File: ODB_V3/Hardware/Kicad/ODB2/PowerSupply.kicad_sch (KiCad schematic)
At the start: 54 parts, among them J15 Vin_XT30PW-F, U13 L6981N33DR, U7 MPQ9843GLE-5-AEC1-Z

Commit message: wip: 3v3 buck
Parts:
- removed NT3: NetTie_2, NetTie:NetTie-2_SMD_Pad0.5mm, symbol Device:NetTie_2
- 3V3_C1, 3V3_C10, 3V3_C2: footprint Capacitor_SMD:C_1210_3225Metric -> Capacitor_SMD:C_0603_1608Metric
- NT4: footprint NetTie:NetTie-2_SMD_Pad0.5mm -> NetTie:NetTie-4_SMD_Pad0.5mm

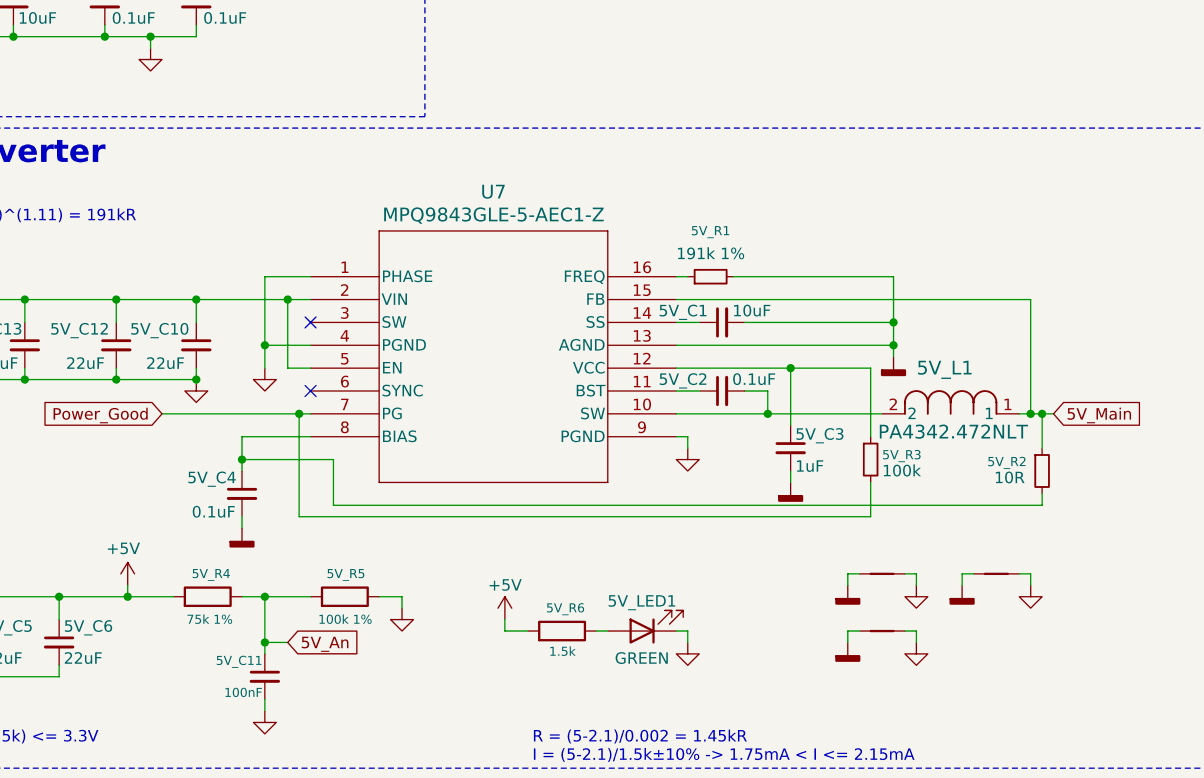
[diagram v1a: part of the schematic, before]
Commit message: feat: add good power input to stm32 + add pull-up 3v3 to good power
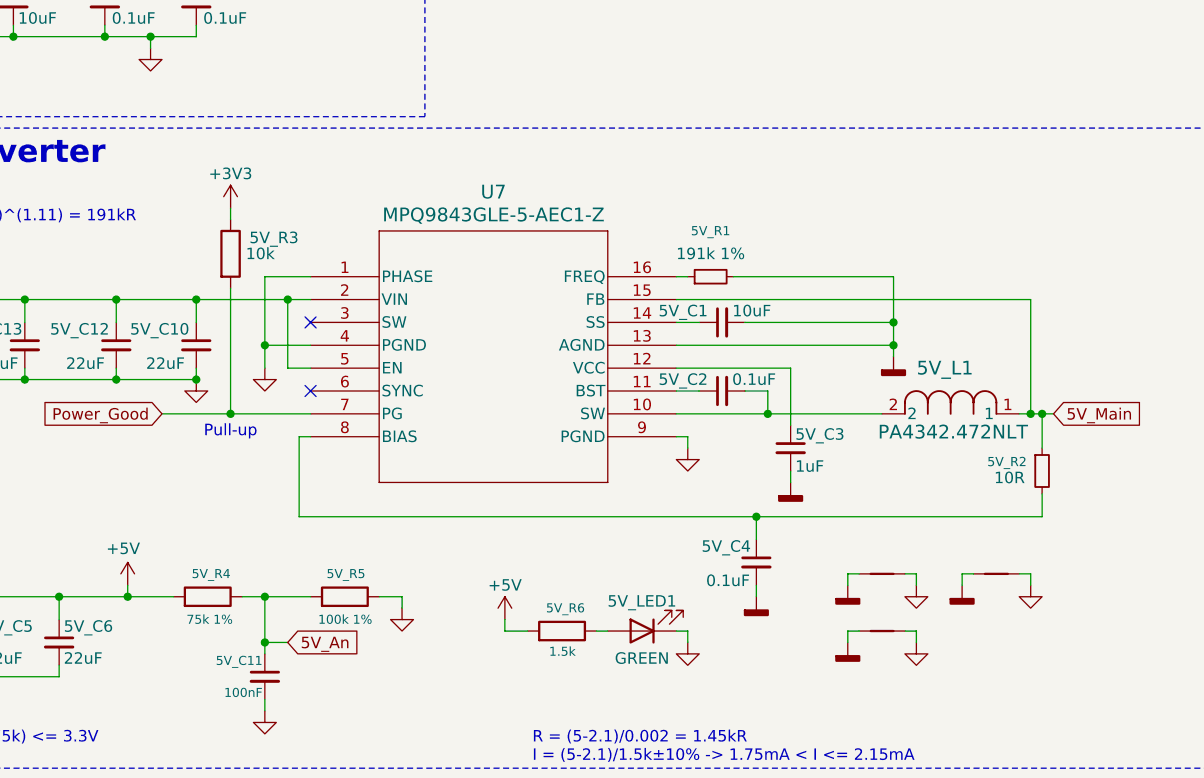
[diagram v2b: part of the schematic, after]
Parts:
- removed 5V_R3: 100k, Resistor_SMD:R_0603_1608Metric, symbol Device:R_Small
- added 5V_R3: 10k, Resistor_SMD:R_0603_1608Metric, symbol Device:R
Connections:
- net +3V3: now also 5V_R3.1
- net Power_Good: now also 5V_R3.2
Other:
- note added: "Pull-up"
- moved on the sheet: 5V_C4

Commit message: wip: pyro trace
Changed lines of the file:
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@@
 	(rectangle
 		(start 15.24 52.07)
-		(end 205.74 123.19)
+		(end 176.53 123.19)
 		(stroke
 			(width 0)

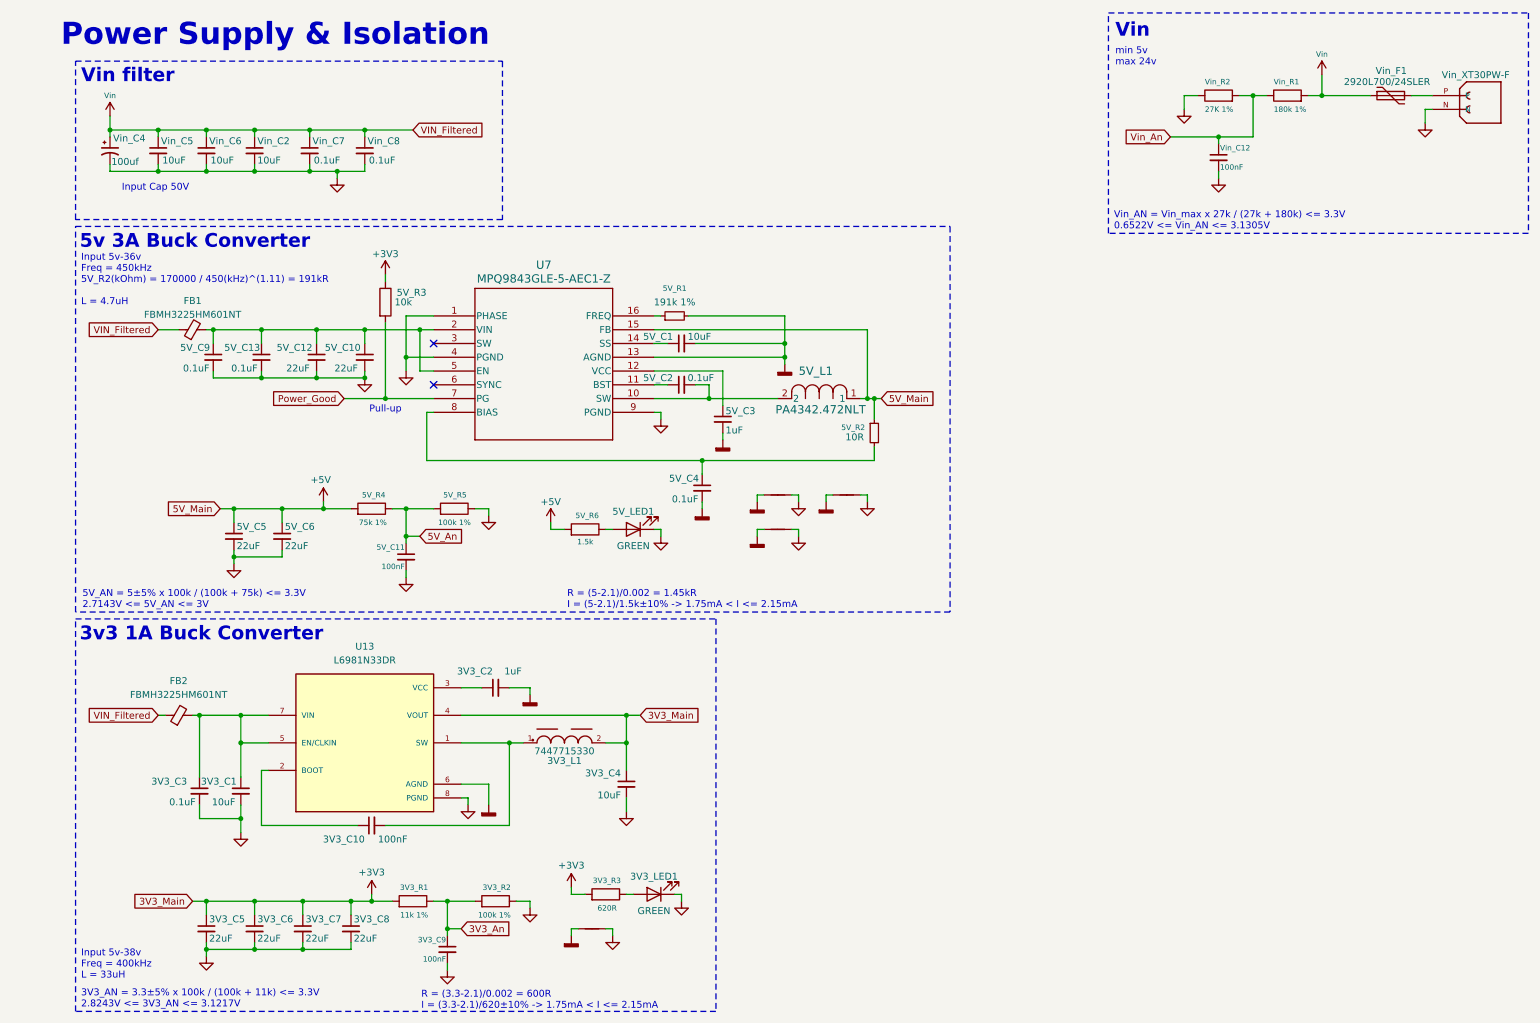
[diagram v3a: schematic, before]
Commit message: wip: change red critical LED to AAKK RG LED + fixes
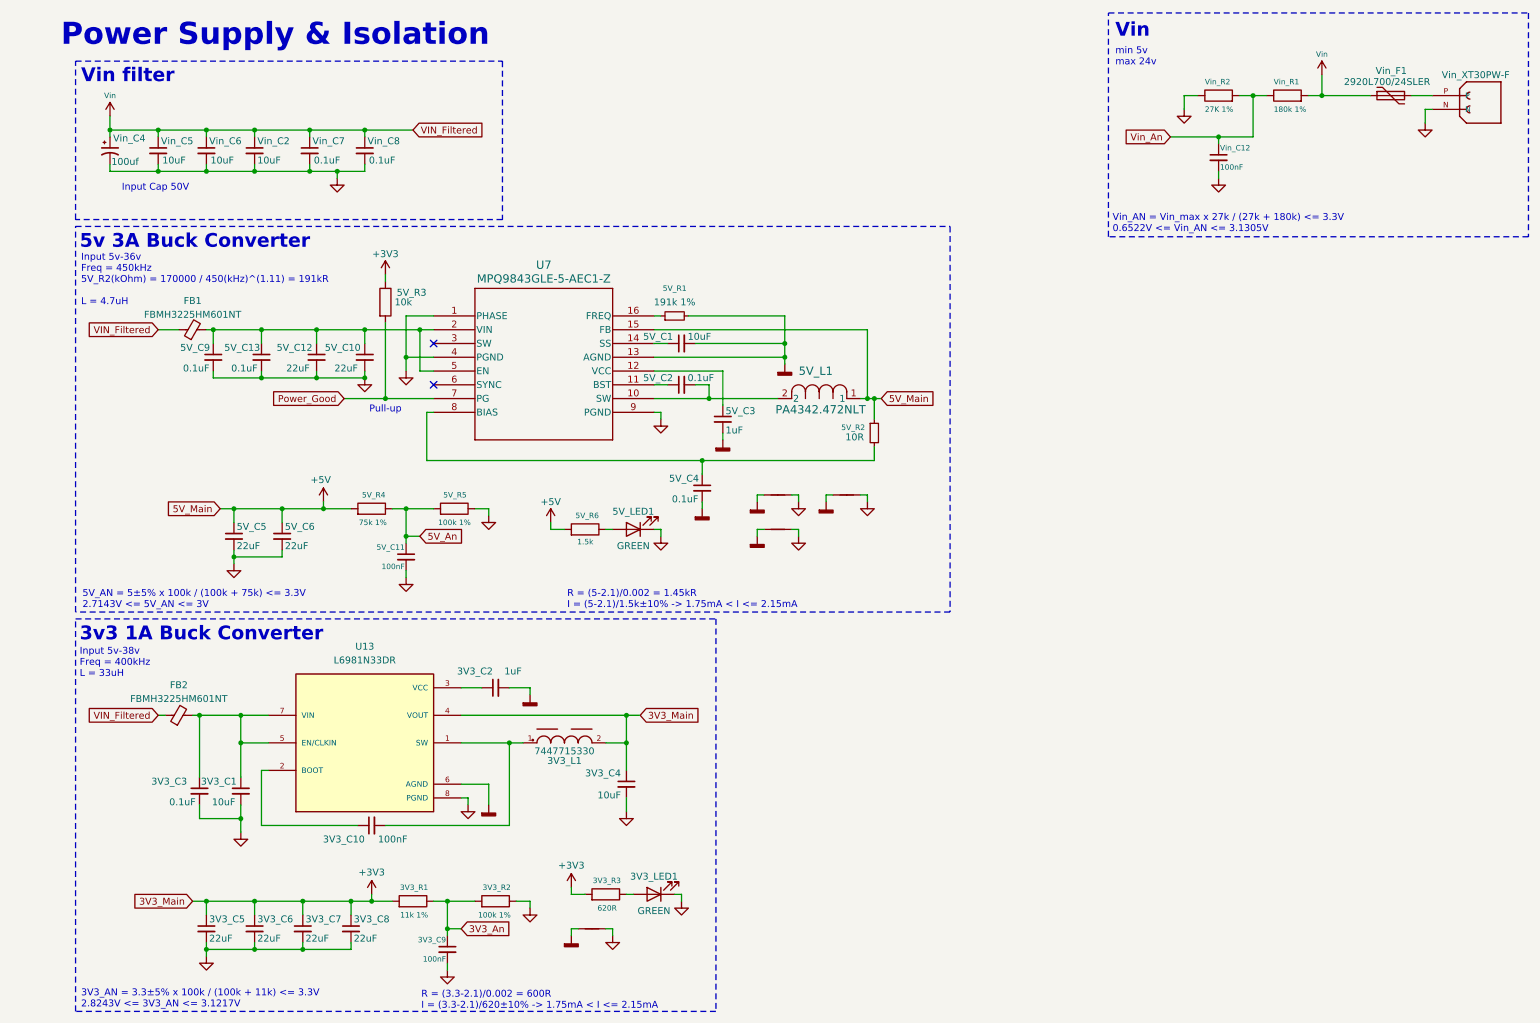
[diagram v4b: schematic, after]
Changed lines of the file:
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@@
 	(rectangle
 		(start 205.74 12.7)
-		(end 283.21 53.34)
+		(end 283.21 53.975)
 		(stroke
 			(width 0)
@@
 	(text "Input 5v-38v\nFreq = 400kHz\nL = 33uH"
 		(exclude_from_sim no)
-		(at 16.256 191.008 0)
+		(at 16.002 135.382 0)
 		(effects
 			(font
@@
 	(text "Vin_AN = Vin_max x 27k / (27k + 180k) <= 3.3V\n0.6522V <= Vin_AN <= 3.1305V"
 		(exclude_from_sim no)
-		(at 206.756 51.054 0)
+		(at 206.502 51.562 0)
 		(effects
 			(font
@@
 		(on_board yes)
 		(dnp no)
-		(fields_autoplaced yes)
 		(property "Reference" "FB2"
-			(at 34.2519 135.89 90)
+			(at 34.29 136.652 90)
 			(effects
 				(font
@@
 		)
 		(property "Value" "FBMH3225HM601NT"
-			(at 34.2519 138.43 90)
+			(at 34.29 139.192 90)
 			(effects
 				(font

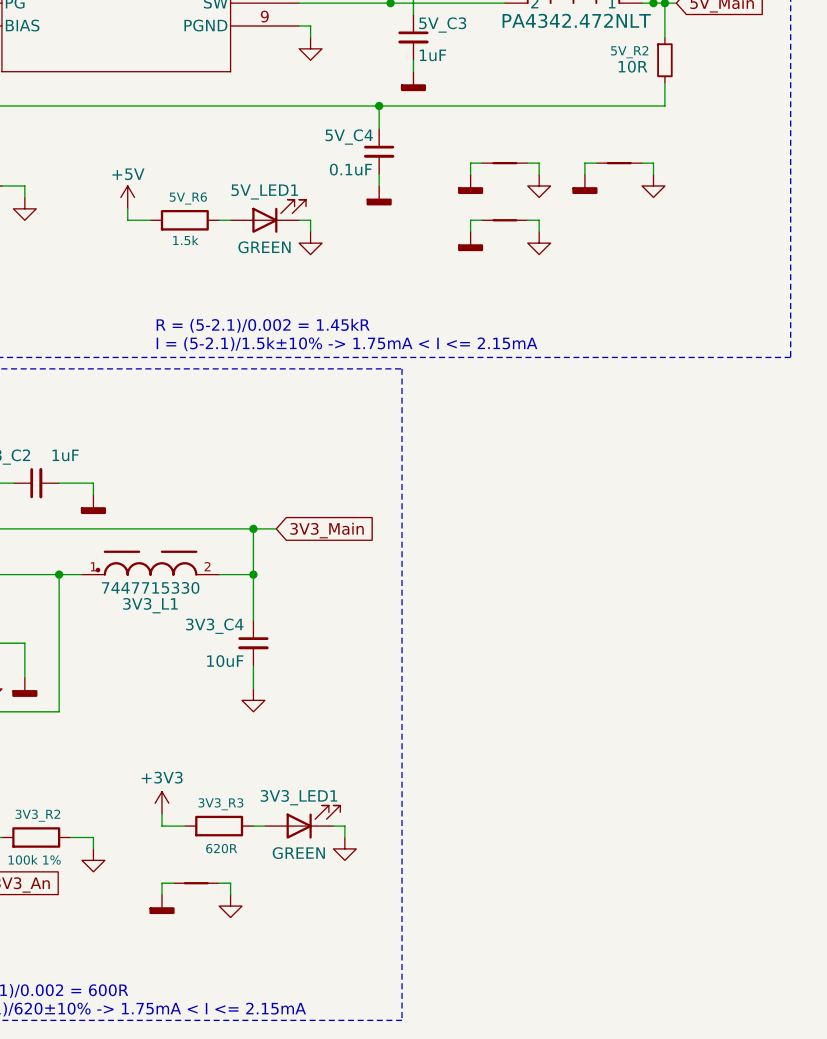
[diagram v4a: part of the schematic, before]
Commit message: fix : remove net-ties from powersupplys
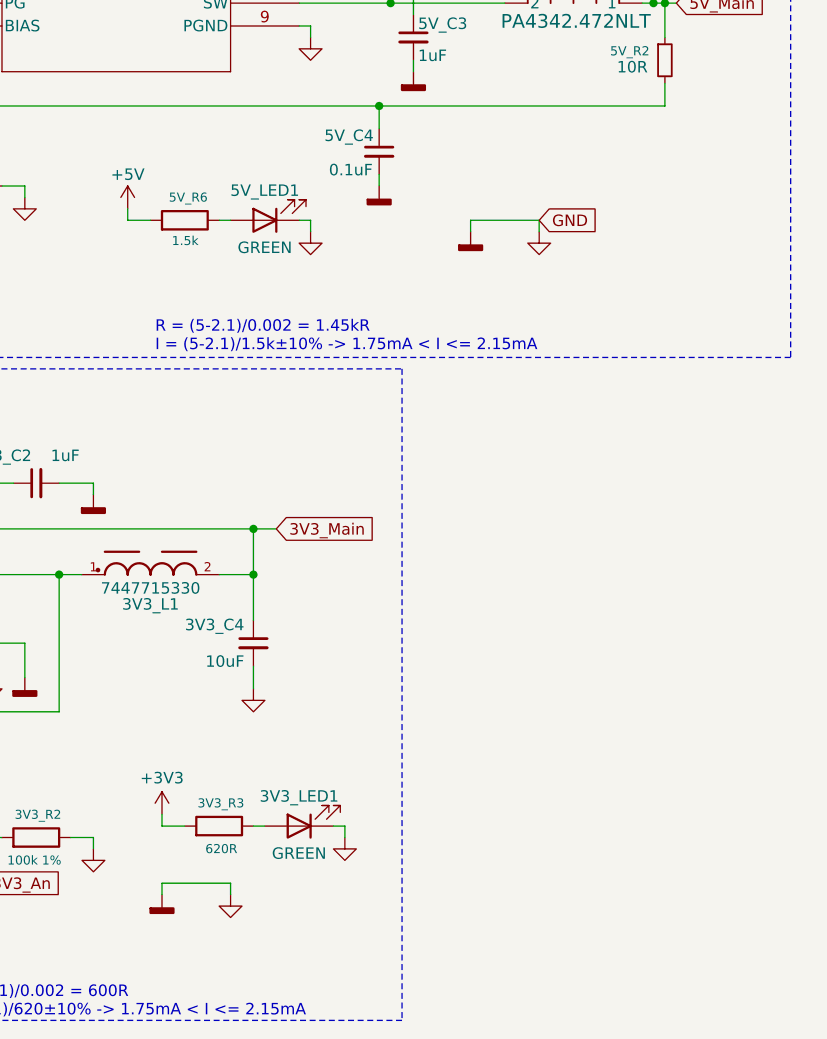
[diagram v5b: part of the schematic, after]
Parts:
- removed NT1, NT2, NT5: NetTie_2, NetTie:NetTie-2_SMD_Pad0.5mm, symbol Device:NetTie_2
- removed NT4: NetTie_2, NetTie:NetTie-4_SMD_Pad0.5mm, symbol Device:NetTie_2
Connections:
- net AGND5V is gone; now on net AGND3V3: 5V_C1.2, 5V_C3.2, 5V_C4.2, 5V_R1.2, U7.13 (AGND)
- net GND is gone; now on net AGND3V3: 3V3_C1.2, 3V3_C3.2, 3V3_C4.2, 3V3_C5.2, 3V3_C6.2, 3V3_C7.2, 3V3_C8.2, 3V3_C9.2, 3V3_LED1.1 (K), 3V3_R2.1, 5V_C10.2, 5V_C11.2, 5V_C12.2, 5V_C13.2, 5V_C5.2, 5V_C6.2, 5V_C9.2, 5V_LED1.1 (K), 5V_R5.1, J15.N, U13.8 (PGND), U7.1 (PHASE), U7.4 (PGND), U7.9 (PGND), Vin_C12.2, Vin_C2.2, Vin_C4.2, Vin_C5.2, Vin_C6.2, Vin_C7.2, Vin_C8.2, Vin_R2.1

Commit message: fix : silkscreen DRC completely done
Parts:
- 5V_C13, 5V_C2, 5V_C4, 5V_C9: footprint Capacitor_SMD:C_0402_1005Metric -> ODB:C_0402_1005Metric
